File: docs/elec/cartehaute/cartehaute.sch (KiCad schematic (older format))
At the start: 12 parts, among them P1 Servo, P10 Analog, P11 ARU, P2 Yeux, P3 LED, P4 HUB, P5 data, P6 5V, P8 AN2, P9 AN1

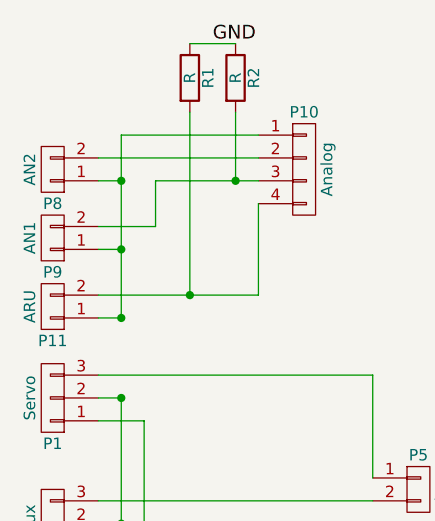
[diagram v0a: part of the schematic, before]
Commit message: ajout svg elec et suppression V1
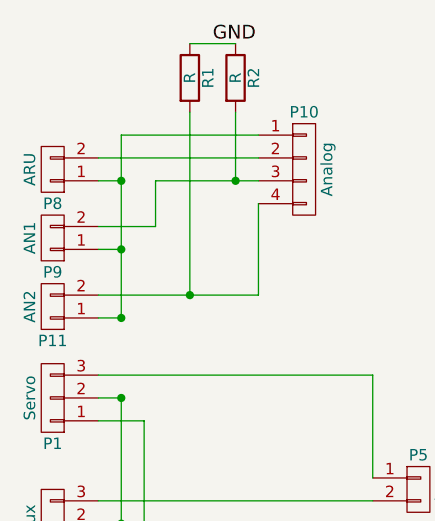
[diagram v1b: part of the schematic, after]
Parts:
- P11: value ARU -> AN2
- P8: value AN2 -> ARU
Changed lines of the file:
@@
 P 3500 2000
 F 0 "P11" H 3500 2150 50  0000 C CNN
-F 1 "ARU" V 3600 2000 50  0000 C CNN
+F 1 "AN2" V 3600 2000 50  0000 C CNN
 F 2 "Pin_Headers:Pin_Header_Straight_1x02" H 3500 2000 50  0001 C CNN
 F 3 "" H 3500 2000 50  0000 C CNN
@@
 P 3500 1400
 F 0 "P8" H 3500 1550 50  0000 C CNN
-F 1 "AN2" V 3600 1400 50  0000 C CNN
+F 1 "ARU" V 3600 1400 50  0000 C CNN
 F 2 "Pin_Headers:Pin_Header_Straight_1x02" H 3500 1400 50  0001 C CNN
 F 3 "" H 3500 1400 50  0000 C CNN

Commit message: update elec
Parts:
- removed P5: data, Pin_Headers:Pin_Header_Straight_1x02, symbol CONN_01X02
- removed R1, R2: R, Wire_Connections_Bridges:WireConnection_1.00mmDrill, symbol R
- added P5: Servo2, Pin_Headers:Pin_Header_Straight_1x03_Pitch2.54mm, symbol CONN_01X03
- added P7: data, Pin_Headers:Pin_Header_Straight_1x03_Pitch2.54mm, symbol CONN_01X03
- P1, P2: footprint Pin_Headers:Pin_Header_Straight_1x03 -> Pin_Headers:Pin_Header_Straight_1x03_Pitch2.54mm
- P10: footprint Pin_Headers:Pin_Header_Straight_1x04 -> Pin_Headers:Pin_Header_Straight_1x04_Pitch2.54mm
- P11, P3, P4, P8, P9: footprint Pin_Headers:Pin_Header_Straight_1x02 -> Pin_Headers:Pin_Header_Straight_1x02_Pitch2.54mm
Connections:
- net 5V: now also P5.2 (P2)
- net GND: now also P5.1 (P1)
- net at P1.3 (P3): now also P7.2 (P2)
- net at P2.3 (P3): now also P7.3 (P3)
- new net: P5.3 (P3), P7.1 (P1)
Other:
- moved on the sheet: P1, P2, P3, P4, P6
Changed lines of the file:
@@
 L CONN_01X02 P3
 U 1 1 581A1274
-P 3500 3450
-F 0 "P3" H 3500 3600 50  0000 C CNN
-F 1 "LED" V 3600 3450 50  0000 C CNN
-F 2 "Pin_Headers:Pin_Header_Straight_1x02" H 3500 3450 50  0001 C CNN
-F 3 "" H 3500 3450 50  0000 C CNN
-	1    3500 3450
+P 3500 3750
+F 0 "P3" H 3500 3900 50  0000 C CNN
+F 1 "LED" V 3600 3750 50  0000 C CNN
+F 2 "Pin_Headers:Pin_Header_Straight_1x02_Pitch2.54mm" H 3500 3750 50  0001 C CNN
+F 3 "" H 3500 3750 50  0000 C CNN
+	1    3500 3750
 	-1   0    0    1
 $EndComp
@@
 L CONN_01X03 P1
 U 1 1 581A12AF
-P 3500 2400
-F 0 "P1" H 3500 2600 50  0000 C CNN
-F 1 "Servo" V 3600 2400 50  0000 C CNN
-F 2 "Pin_Headers:Pin_Header_Straight_1x03" H 3500 2400 50  0001 C CNN
-F 3 "" H 3500 2400 50  0000 C CNN
-	1    3500 2400
+P 3500 2700
+F 0 "P1" H 3500 2900 50  0000 C CNN
+F 1 "Servo" V 3600 2700 50  0000 C CNN
+F 2 "Pin_Headers:Pin_Header_Straight_1x03_Pitch2.54mm" H 3500 2700 50  0001 C CNN
+F 3 "" H 3500 2700 50  0000 C CNN
+	1    3500 2700
 	-1   0    0    1
 $EndComp
@@
 L CONN_01X03 P2
 U 1 1 581A12FA
-P 3500 2950
-F 0 "P2" H 3500 3150 50  0000 C CNN
-F 1 "Yeux" V 3600 2950 50  0000 C CNN
-F 2 "Pin_Headers:Pin_Header_Straight_1x03" H 3500 2950 50  0001 C CNN
-F 3 "" H 3500 2950 50  0000 C CNN
-	1    3500 2950
+P 3500 3250
+F 0 "P2" H 3500 3450 50  0000 C CNN
+F 1 "Yeux" V 3600 3250 50  0000 C CNN
+F 2 "Pin_Headers:Pin_Header_Straight_1x03_Pitch2.54mm" H 3500 3250 50  0001 C CNN
+F 3 "" H 3500 3250 50  0000 C CNN
+	1    3500 3250
 	-1   0    0    1
 $EndComp
@@
 L CONN_01X02 P4
 U 1 1 581A1378
-P 3500 3850
-F 0 "P4" H 3500 4000 50  0000 C CNN
-F 1 "HUB" V 3600 3850 50  0000 C CNN
-F 2 "Pin_Headers:Pin_Header_Straight_1x02" H 3500 3850 50  0001 C CNN
-F 3 "" H 3500 3850 50  0000 C CNN
-	1    3500 3850
+P 3500 4150
+F 0 "P4" H 3500 4300 50  0000 C CNN
+F 1 "HUB" V 3600 4150 50  0000 C CNN
+F 2 "Pin_Headers:Pin_Header_Straight_1x02_Pitch2.54mm" H 3500 4150 50  0001 C CNN
+F 3 "" H 3500 4150 50  0000 C CNN
+	1    3500 4150
 	-1   0    0    1
 $EndComp
@@
 L CONN_01X02 P6
 U 1 1 581A13A0
-P 5100 3450
-F 0 "P6" H 5100 3600 50  0000 C CNN
-F 1 "5V" V 5200 3450 50  0000 C CNN
-F 2 "robair:Bornier5mm" H 5100 3450 50  0001 C CNN
-F 3 "" H 5100 3450 50  0000 C CNN
-	1    5100 3450
+P 5100 3750
+F 0 "P6" H 5100 3900 50  0000 C CNN
+F 1 "5V" V 5200 3750 50  0000 C CNN
+F 2 "robair:Bornier5mm" H 5100 3750 50  0001 C CNN
+F 3 "" H 5100 3750 50  0000 C CNN
+	1    5100 3750
 	1    0    0    1
 $EndComp
@@
 F 0 "P11" H 3500 2150 50  0000 C CNN
 F 1 "AN2" V 3600 2000 50  0000 C CNN
-F 2 "Pin_Headers:Pin_Header_Straight_1x02" H 3500 2000 50  0001 C CNN
+F 2 "Pin_Headers:Pin_Header_Straight_1x02_Pitch2.54mm" H 3500 2000 50  0001 C CNN
 F 3 "" H 3500 2000 50  0000 C CNN
 	1    3500 2000
 	-1   0    0    1
-$EndComp
-$Comp
-L CONN_01X02 P5
-U 1 1 581A14B9
-P 5100 2800
-F 0 "P5" H 5100 2950 50  0000 C CNN
-F 1 "data" V 5200 2800 50  0000 C CNN
-F 2 "Pin_Headers:Pin_Header_Straight_1x02" H 5100 2800 50  0001 C CNN
-F 3 "" H 5100 2800 50  0000 C CNN
-	1    5100 2800
-	1    0    0    -1
 $EndComp
 $Comp
@@
 F 0 "P9" H 3500 1850 50  0000 C CNN
 F 1 "AN1" V 3600 1700 50  0000 C CNN
-F 2 "Pin_Headers:Pin_Header_Straight_1x02" H 3500 1700 50  0001 C CNN
+F 2 "Pin_Headers:Pin_Header_Straight_1x02_Pitch2.54mm" H 3500 1700 50  0001 C CNN
 F 3 "" H 3500 1700 50  0000 C CNN
 	1    3500 1700
@@
 F 0 "P8" H 3500 1550 50  0000 C CNN
 F 1 "ARU" V 3600 1400 50  0000 C CNN
-F 2 "Pin_Headers:Pin_Header_Straight_1x02" H 3500 1400 50  0001 C CNN
+F 2 "Pin_Headers:Pin_Header_Straight_1x02_Pitch2.54mm" H 3500 1400 50  0001 C CNN
 F 3 "" H 3500 1400 50  0000 C CNN
 	1    3500 1400
@@
 F 0 "P10" H 4600 1650 50  0000 C CNN
 F 1 "Analog" V 4700 1400 50  0000 C CNN
-F 2 "Pin_Headers:Pin_Header_Straight_1x04" H 4600 1400 50  0001 C CNN
+F 2 "Pin_Headers:Pin_Header_Straight_1x04_Pitch2.54mm" H 4600 1400 50  0001 C CNN
 F 3 "" H 4600 1400 50  0000 C CNN
 	1    4600 1400
 	1    0    0    -1
 $EndComp
-Text Label 4300 3400 0    60   ~ 0
+Text Label 4300 3700 0    60   ~ 0
 5V
-Text Label 4300 3500 0    60   ~ 0
+Text Label 4300 3800 0    60   ~ 0
 GND
 Wire Wire Line
-	3900 2500 3900 3900
+	3900 2450 3900 4200
 Wire Wire Line
-	3900 3900 3700 3900
-Connection ~ 3900 3500
+	3900 4200 3700 4200
+Connection ~ 3900 3800
 Wire Wire Line
-	3800 3800 3700 3800
+	3800 4100 3700 4100
 Wire Wire Line
-	3700 3400 4900 3400
+	3700 3700 4900 3700
 Wire Wire Line
-	3900 3050 3700 3050
+	3900 3350 3700 3350
 Wire Wire Line
-	3900 2500 3700 2500
-Connection ~ 3900 3050
+	3900 2800 3700 2800
+Connection ~ 3900 3350
 Wire Wire Line
-	3700 3500 4900 3500
-Connection ~ 3800 3400
+	3700 3800 4900 3800
+Connection ~ 3800 3700
 Wire Wire Line
-	3800 2950 3700 2950
+	3800 3250 3700 3250
 Wire Wire Line
-	3800 2400 3700 2400
-Connection ~ 3800 2950
+	3800 2700 3700 2700
+Connection ~ 3800 3250
 Wire Wire Line
-	4900 2850 3700 2850
+	3700 3150 4950 3150
 Wire Wire Line
-	4900 2750 4900 2300
+	4900 3050 4900 2600
 Wire Wire Line
-	4900 2300 3700 2300
+	4900 2600 3700 2600
 Wire Wire Line
 	3800 2050 3700 2050
-Connection ~ 3800 2400
+Connection ~ 3800 2700
 Wire Wire Line
 	3800 1750 3700 1750
@@
 	3800 1250 3800 2050
 Wire Wire Line
-	3800 2400 3800 3800
+	3800 2350 3800 4100
 $Comp
-L R R1
-U 1 1 582EF7E3
-P 4100 1000
-F 0 "R1" V 4180 1000 50  0000 C CNN
-F 1 "R" V 4100 1000 50  0000 C CNN
-F 2 "Wire_Connections_Bridges:WireConnection_1.00mmDrill" V 4030 1000 50  0001 C CNN
-F 3 "" H 4100 1000 50  0000 C CNN
-	1    4100 1000
-	1    0    0    -1
+L CONN_01X03 P5
+U 1 1 58CB0AEB
+P 3500 2350
+F 0 "P5" H 3500 2550 50  0000 C CNN
+F 1 "Servo2" V 3600 2350 50  0000 C CNN
+F 2 "Pin_Headers:Pin_Header_Straight_1x03_Pitch2.54mm" H 3500 2350 50  0001 C CNN
+F 3 "" H 3500 2350 50  0000 C CNN
+	1    3500 2350
+	-1   0    0    1
 $EndComp
 $Comp
-L R R2
-U 1 1 582EF867
-P 4300 1000
-F 0 "R2" V 4380 1000 50  0000 C CNN
-F 1 "R" V 4300 1000 50  0000 C CNN
-F 2 "Wire_Connections_Bridges:WireConnection_1.00mmDrill" V 4230 1000 50  0001 C CNN
-F 3 "" H 4300 1000 50  0000 C CNN
-	1    4300 1000
+L CONN_01X03 P7
+U 1 1 58CB0F48
+P 5150 3050
+F 0 "P7" H 5150 3250 50  0000 C CNN
+F 1 "data" V 5250 3050 50  0000 C CNN
+F 2 "Pin_Headers:Pin_Header_Straight_1x03_Pitch2.54mm" H 5150 3050 50  0001 C CNN
+F 3 "" H 5150 3050 50  0000 C CNN
+	1    5150 3050
 	1    0    0    -1
 $EndComp
 Wire Wire Line
-	4100 850  4300 850
+	3700 2350 3800 2350
 Wire Wire Line
-	4100 1150 4100 1950
-Connection ~ 4100 1950
+	3700 2450 3900 2450
+Connection ~ 3900 2800
 Wire Wire Line
-	4300 1150 4300 1450
-Connection ~ 4300 1450
-Text Label 4200 850  0    60   ~ 0
-GND
+	4950 3050 4900 3050
+Wire Wire Line
+	4950 2950 4950 2250
+Wire Wire Line
+	4950 2250 3700 2250
 $EndSCHEMATC

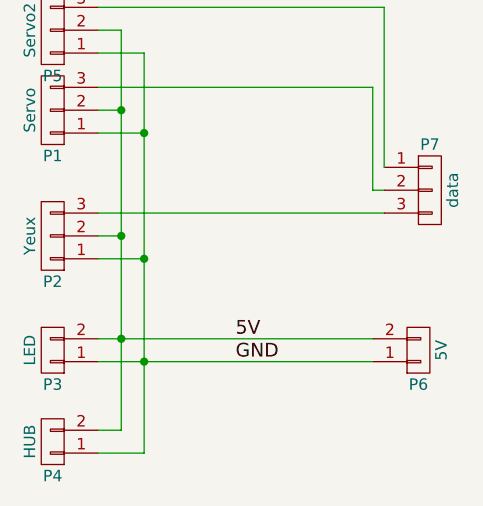
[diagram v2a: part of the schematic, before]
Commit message: Ajoute les connecteurs 12 et 19V sur la carte haute
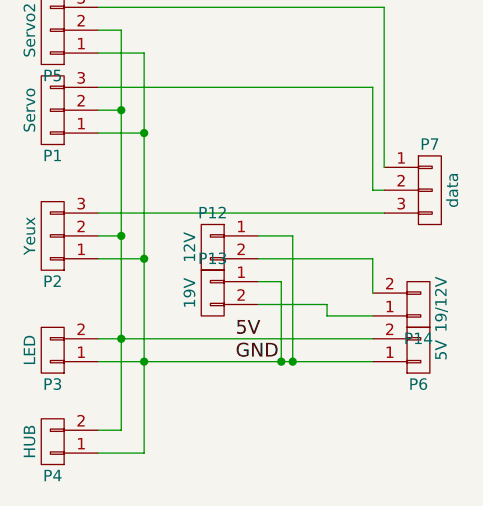
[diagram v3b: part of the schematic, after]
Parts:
- added P12: 12V, robair:Bornier5mm, symbol CONN_01X02
- added P13: 19V, robair:Bornier5mm, symbol CONN_01X02
- added P14: 19/12V, robair:Bornier5mm, symbol CONN_01X02
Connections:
- net GND: now also P12.1 (P1), P13.1 (P1)
- new net: P13.2 (P2), P14.1 (P1)
- new net: P12.2 (P2), P14.2 (P2)
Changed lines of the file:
@@
 Text Label 4300 3800 0    60   ~ 0
 GND
+$Comp
+L CONN_01X03 P5
+U 1 1 58CB0AEB
+P 3500 2350
+F 0 "P5" H 3500 2550 50  0000 C CNN
+F 1 "Servo2" V 3600 2350 50  0000 C CNN
+F 2 "Pin_Headers:Pin_Header_Straight_1x03_Pitch2.54mm" H 3500 2350 50  0001 C CNN
+F 3 "" H 3500 2350 50  0000 C CNN
+	1    3500 2350
+	-1   0    0    1
+$EndComp
+$Comp
+L CONN_01X03 P7
+U 1 1 58CB0F48
+P 5150 3050
+F 0 "P7" H 5150 3250 50  0000 C CNN
+F 1 "data" V 5250 3050 50  0000 C CNN
+F 2 "Pin_Headers:Pin_Header_Straight_1x03_Pitch2.54mm" H 5150 3050 50  0001 C CNN
+F 3 "" H 5150 3050 50  0000 C CNN
+	1    5150 3050
+	1    0    0    -1
+$EndComp
+$Comp
+L CONN_01X02 P14
+U 1 1 59CBA5A8
+P 5100 3550
+F 0 "P14" H 5100 3700 50  0000 C CNN
+F 1 "19/12V" V 5200 3550 50  0000 C CNN
+F 2 "robair:Bornier5mm" H 5100 3550 50  0001 C CNN
+F 3 "" H 5100 3550 50  0000 C CNN
+	1    5100 3550
+	1    0    0    1
+$EndComp
+$Comp
+L CONN_01X02 P12
+U 1 1 59CBA6DE
+P 4200 3300
+F 0 "P12" H 4200 3450 50  0000 C CNN
+F 1 "12V" V 4300 3300 50  0000 C CNN
+F 2 "robair:Bornier5mm" H 4200 3300 50  0001 C CNN
+F 3 "" H 4200 3300 50  0000 C CNN
+	1    4200 3300
+	-1   0    0    -1
+$EndComp
+$Comp
+L CONN_01X02 P13
+U 1 1 59CBA743
+P 4200 3500
+F 0 "P13" H 4200 3650 50  0000 C CNN
+F 1 "19V" V 4300 3500 50  0000 C CNN
+F 2 "robair:Bornier5mm" H 4200 3500 50  0001 C CNN
+F 3 "" H 4200 3500 50  0000 C CNN
+	1    4200 3500
+	-1   0    0    -1
+$EndComp
 Wire Wire Line
 	3900 2450 3900 4200
@@
 Wire Wire Line
 	3800 2350 3800 4100
-$Comp
-L CONN_01X03 P5
-U 1 1 58CB0AEB
-P 3500 2350
-F 0 "P5" H 3500 2550 50  0000 C CNN
-F 1 "Servo2" V 3600 2350 50  0000 C CNN
-F 2 "Pin_Headers:Pin_Header_Straight_1x03_Pitch2.54mm" H 3500 2350 50  0001 C CNN
-F 3 "" H 3500 2350 50  0000 C CNN
-	1    3500 2350
-	-1   0    0    1
-$EndComp
-$Comp
-L CONN_01X03 P7
-U 1 1 58CB0F48
-P 5150 3050
-F 0 "P7" H 5150 3250 50  0000 C CNN
-F 1 "data" V 5250 3050 50  0000 C CNN
-F 2 "Pin_Headers:Pin_Header_Straight_1x03_Pitch2.54mm" H 5150 3050 50  0001 C CNN
-F 3 "" H 5150 3050 50  0000 C CNN
-	1    5150 3050
-	1    0    0    -1
-$EndComp
 Wire Wire Line
 	3700 2350 3800 2350
@@
 Wire Wire Line
 	4950 2250 3700 2250
+Wire Wire Line
+	4500 3800 4500 3450
+Wire Wire Line
+	4500 3450 4400 3450
+Connection ~ 4500 3800
+Wire Wire Line
+	4550 3800 4550 3250
+Wire Wire Line
+	4550 3250 4400 3250
+Connection ~ 4550 3800
+Wire Wire Line
+	4900 3600 4700 3600
+Wire Wire Line
+	4700 3600 4700 3550
+Wire Wire Line
+	4700 3550 4400 3550
+Wire Wire Line
+	4900 3500 4900 3350
+Wire Wire Line
+	4900 3350 4400 3350
 $EndSCHEMATC

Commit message: Simplify the top board
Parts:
- removed P10: Analog, Pin_Headers:Pin_Header_Straight_1x04_Pitch2.54mm, symbol CONN_01X04
- removed P11: AN2, Pin_Headers:Pin_Header_Straight_1x02_Pitch2.54mm, symbol CONN_01X02
- removed P12: 12V, robair:Bornier5mm, symbol CONN_01X02
- removed P13: 19V, robair:Bornier5mm, symbol CONN_01X02
- removed P14: 19/12V, robair:Bornier5mm, symbol CONN_01X02
- removed P3: LED, Pin_Headers:Pin_Header_Straight_1x02_Pitch2.54mm, symbol CONN_01X02
- removed P4: HUB, Pin_Headers:Pin_Header_Straight_1x02_Pitch2.54mm, symbol CONN_01X02
- removed P6: 5V, robair:Bornier5mm, symbol CONN_01X02
- removed P7: data, Pin_Headers:Pin_Header_Straight_1x03_Pitch2.54mm, symbol CONN_01X03
- removed P8: ARU, Pin_Headers:Pin_Header_Straight_1x02_Pitch2.54mm, symbol CONN_01X02
- removed P9: AN1, Pin_Headers:Pin_Header_Straight_1x02_Pitch2.54mm, symbol CONN_01X02
- added P3: D3, Pin_Headers:Pin_Header_Straight_1x03_Pitch2.54mm, symbol conn:CONN_01X03
- added P4: D4, Pin_Headers:Pin_Header_Straight_1x03_Pitch2.54mm, symbol conn:CONN_01X03
- added P6, P8: CONN_01X02, Connectors_Phoenix:PhoenixContact_MC-G_02x5.08mm_Angled, symbol conn:CONN_01X02
- added P7: CONN_01X05, Pin_Headers:Pin_Header_Straight_1x05_Pitch2.54mm, symbol conn:CONN_01X05
- P1: value Servo -> D1; symbol CONN_01X03 -> conn:CONN_01X03
- P2: value Yeux -> D2; symbol CONN_01X03 -> conn:CONN_01X03
- P5: value Servo2 -> D5; symbol CONN_01X03 -> conn:CONN_01X03
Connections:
- wire segments 38 -> 40
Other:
- moved on the sheet: P1, P2, P5
